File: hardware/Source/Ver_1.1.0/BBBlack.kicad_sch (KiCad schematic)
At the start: 11 parts

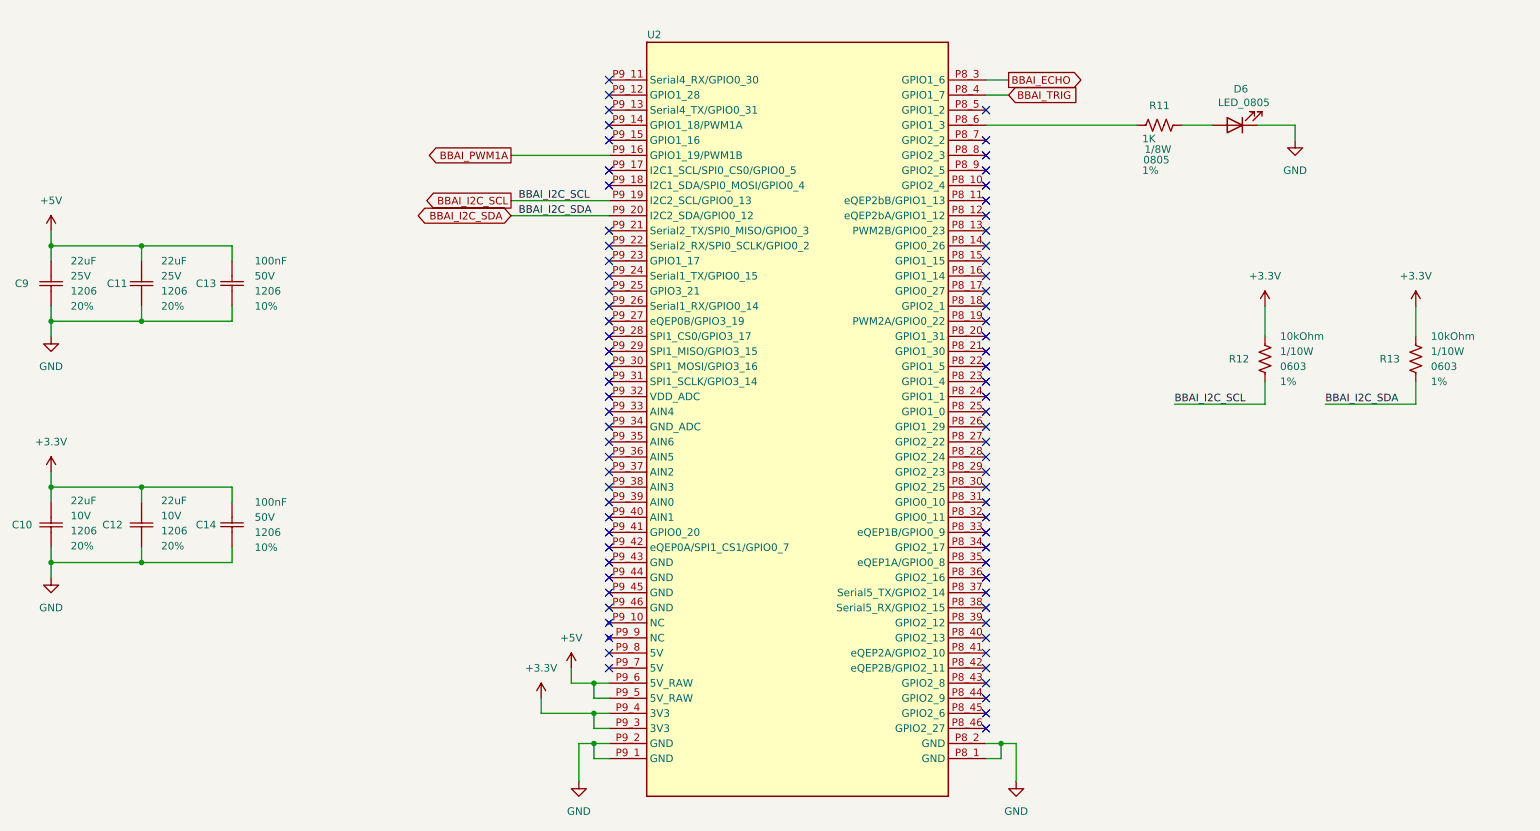
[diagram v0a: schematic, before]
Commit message: Generate PDF Schematic Ver1.1.0 and add README.md
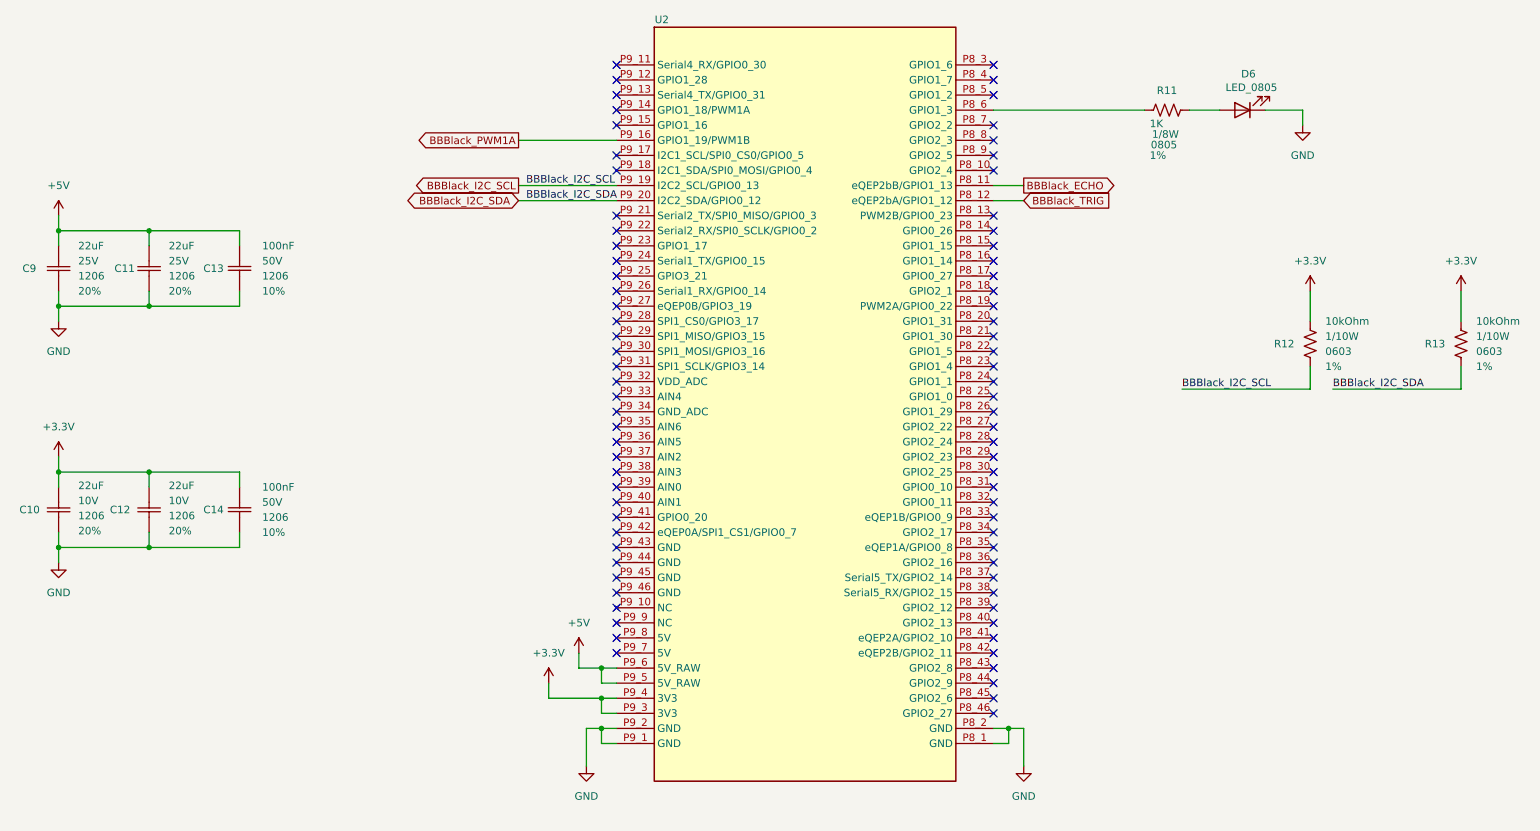
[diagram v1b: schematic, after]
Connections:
- net BBBlack_ECHO: now reaches U2.P8_11 (eQEP2bB/GPIO1_13)
- net BBBlack_TRIG: now reaches U2.P8_12 (eQEP2bA/GPIO1_12)
- net BBAI_ECHO: no longer names the net of U2.P8_3 (GPIO1_6)
- net BBAI_I2C_SCL renamed BBBlack_I2C_SCL
- net BBAI_I2C_SDA renamed BBBlack_I2C_SDA
- net BBAI_PWM1A renamed BBBlack_PWM1A
- net BBAI_TRIG: no longer names the net of U2.P8_4 (GPIO1_7)
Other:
- title: BBAI -> (none)
- moved on the sheet: C10, C11, C12, C13, C14, C9, D6, R11, R12, R13, U2
